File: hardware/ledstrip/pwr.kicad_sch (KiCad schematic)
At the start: 48 parts, among them J4 BMS connectors, J6 Header for STUSB4500 I2C, Q4 Q_PMOS, Q5 Q_NMOS, Q6 Q_NMOS, Q7 Q_NMOS, Q8 Q_NMOS, U5 BQ25703A, U6 STUSB4500QTR

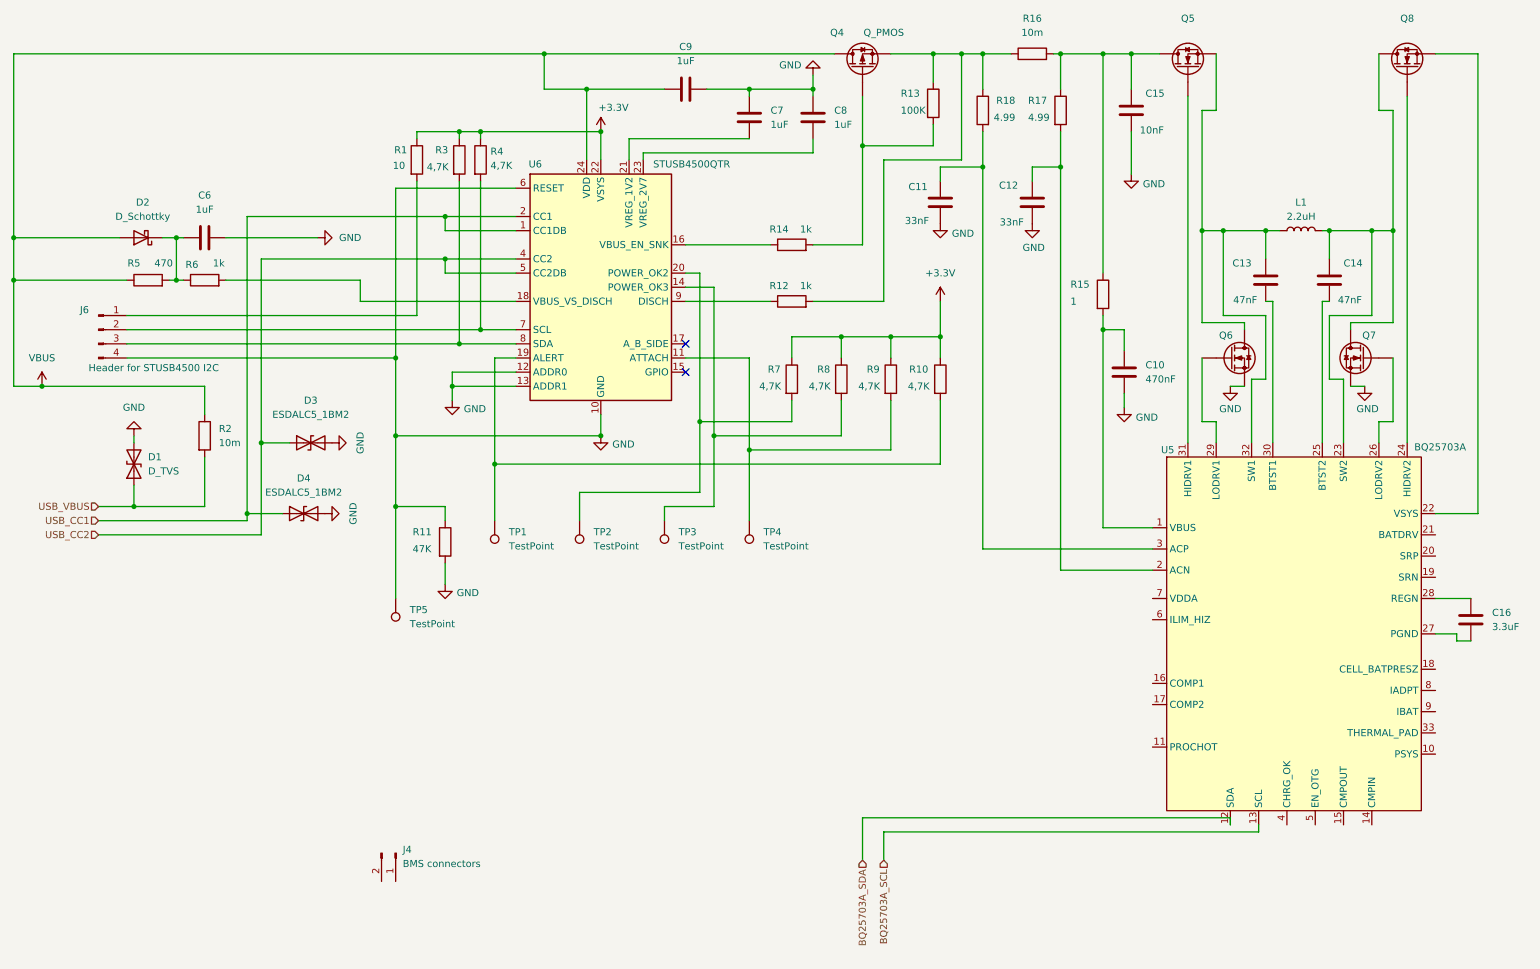
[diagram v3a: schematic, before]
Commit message: Splitted into multiple sheets.
BQ25703A integrated
buck converter OK
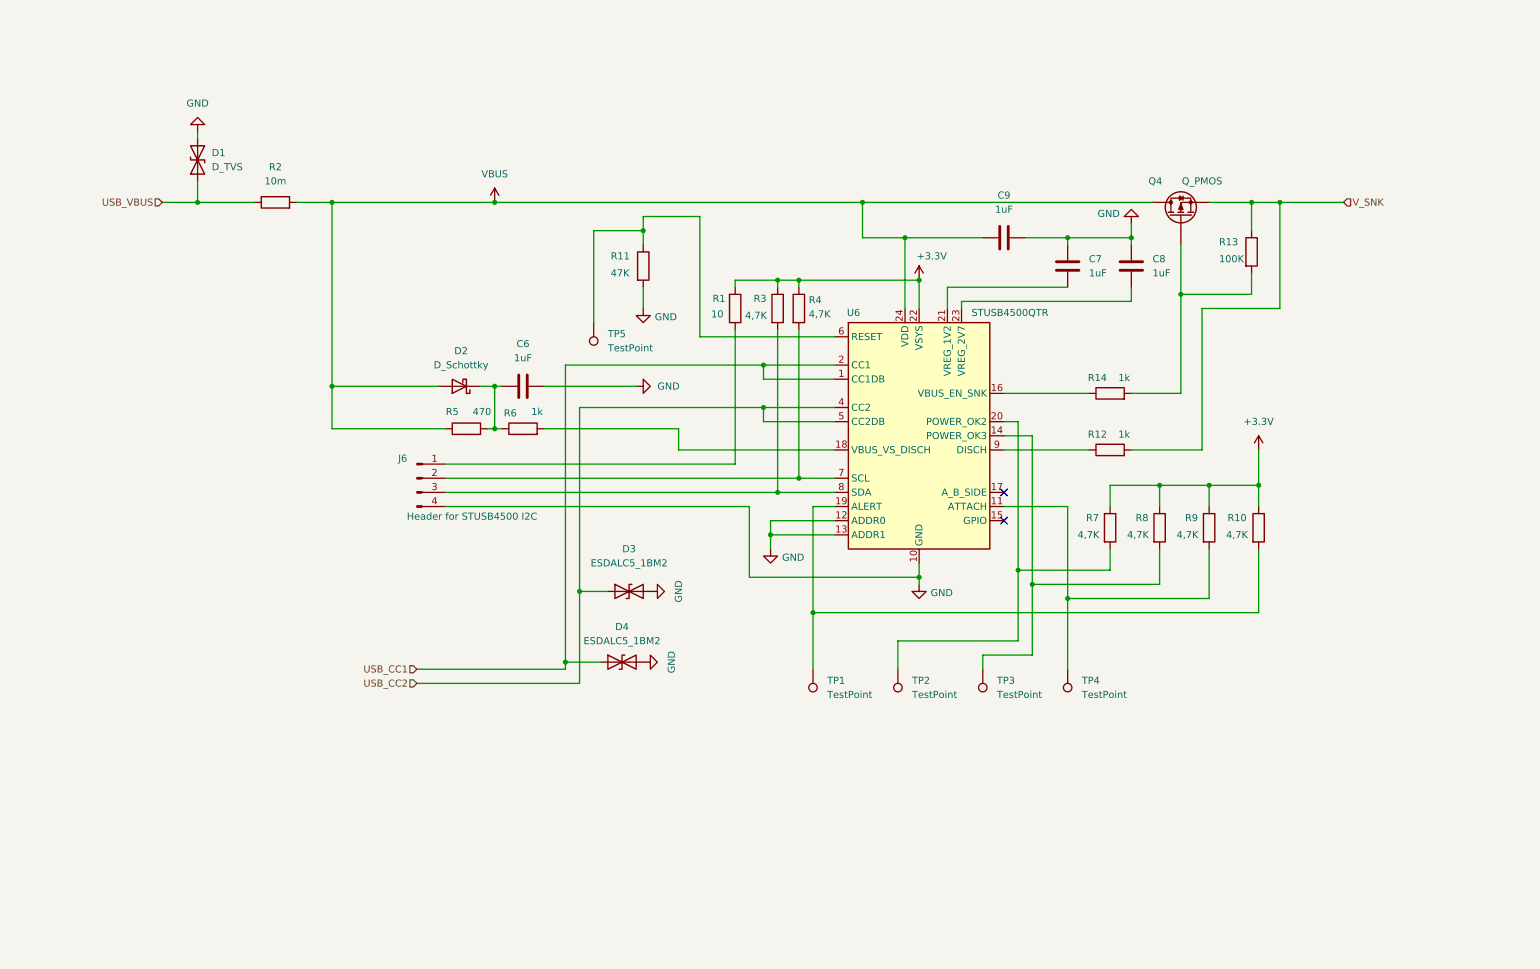
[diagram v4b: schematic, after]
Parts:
- removed C10: 470nF, Capacitor_SMD:C_0603_1608Metric, symbol Device:C
- removed C11, C12: 33nF, Capacitor_SMD:C_0603_1608Metric, symbol Device:C
- removed C13, C14: 47nF, Capacitor_SMD:C_0603_1608Metric, symbol Device:C
- removed C15: 10nF, Capacitor_SMD:C_0603_1608Metric, symbol Device:C
- removed C16: 3.3uF, Capacitor_SMD:C_0603_1608Metric, symbol Device:C
- removed J4: BMS connectors, Connector_PinHeader_2.54mm:PinHeader_1x02_P2.54mm_Vertical, symbol Connector:Conn_01x02_Pin
- removed L1: 2.2uH, ledstrip:L_Wurth_WE-LHMI-8030_9.7x8.5mm, symbol Device:L
- removed Q5, Q6, Q7, Q8: Q_NMOS, Package_SON:VSON-8_3.3x3.3mm_P0.65mm_NexFET, symbol Device:Q_NMOS
- removed R15: 1, Resistor_SMD:R_0805_2012Metric, symbol Device:R
- removed R16: 10m, Resistor_SMD:R_0805_2012Metric, symbol Device:R
- removed R17, R18: 4.99, Resistor_SMD:R_0805_2012Metric, symbol Device:R
- removed U5: BQ25703A, Package_DFN_QFN:Texas_RSN_WQFN-32-1EP_4x4mm_P0.4mm_EP2.8x2.8mm_ThermalVias, symbol ledstrip:BQ25703A
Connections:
- net GND: no longer R11.1, TP5.1, U6.6 (RESET)
- net USB_VBUS: now also R2.1; no longer R2.2
- net VBUS: now also R2.2; no longer R2.1
- net V_SNK: now reaches Q4.S, R12.2, R13.1
- new net: R11.1, TP5.1, U6.6 (RESET)
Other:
- moved on the sheet: C6, C7, C8, C9, D1, D2, D3, D4, J6, Q4, R1, R10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

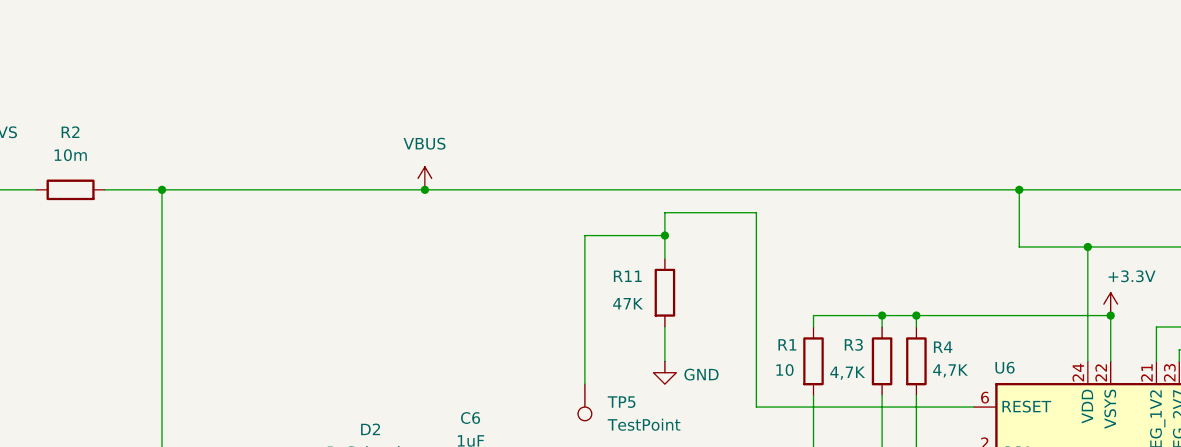
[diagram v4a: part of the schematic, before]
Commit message: Fix ERC errors.
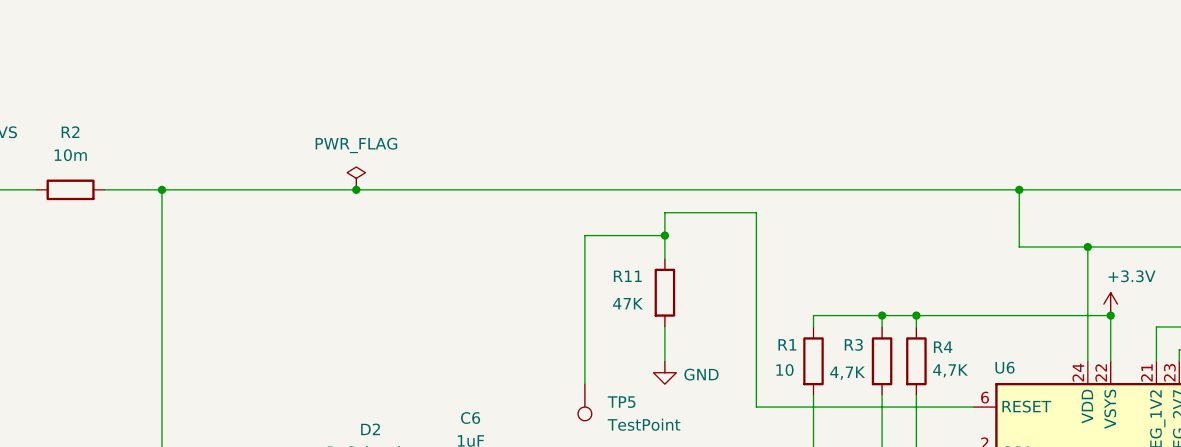
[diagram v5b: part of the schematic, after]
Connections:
- net VBUS: no longer names the net of C9.1, D2.2 (A), Q4.D, R2.2, R5.1, U6.24 (VDD)
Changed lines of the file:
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@@
 	)
 	(junction
+		(at 92.71 44.45)
+		(diameter 0)
+		(color 0 0 0 0)
+	)
+	(junction
 		(at 173.99 50.8)
 		(diameter 0)
@@
 	)
 	(junction
-		(at 100.33 44.45)
-		(diameter 0)
-		(color 0 0 0 0)
-	)
-	(junction
 		(at 71.12 44.45)
 		(diameter 0)
@@
 	(wire
 		(pts
-			(xy 100.33 44.45) (xy 166.37 44.45)
+			(xy 92.71 44.45) (xy 166.37 44.45)
 		)
 		(stroke
@@
 	(wire
 		(pts
-			(xy 71.12 44.45) (xy 100.33 44.45)
+			(xy 71.12 44.45) (xy 92.71 44.45)
 		)
 		(stroke
@@
 	)
 	(symbol
-		(lib_id "power:VBUS")
-		(at 100.33 44.45 0)
-		(unit 1)
-		(exclude_from_sim no)
-		(in_bom yes)
-		(on_board yes)
-		(dnp no)
-		(fields_autoplaced yes)
-		(property "Reference" "#PWR028"
-			(at 100.33 48.26 0)
-			(effects
-				(font
-					(size 1.27 1.27)
-				)
-				(hide yes)
-			)
-		)
-		(property "Value" "VBUS"
-			(at 100.33 39.37 0)
-			(effects
-				(font
-					(size 1.27 1.27)
-				)
-			)
-		)
-		(property "Footprint" ""
-			(at 100.33 44.45 0)
-			(effects
-				(font
-					(size 1.27 1.27)
-				)
-				(hide yes)
-			)
-		)
-		(property "Datasheet" ""
-			(at 100.33 44.45 0)
-			(effects
-				(font
-					(size 1.27 1.27)
-				)
-				(hide yes)
-			)
-		)
-		(property "Description" "Power symbol creates a global label with name \"VBUS\""
-			(at 100.33 44.45 0)
-			(effects
-				(font
-					(size 1.27 1.27)
-				)
-				(hide yes)
-			)
-		)
-		(pin "1"
-		)
-		(instances
-			(project "ledstrip"
-				(path "/dcb997ee-94c4-4df2-ba22-0e091735ddd7/b5cca531-fcff-4497-988a-ecdd56b3ddf9"
-					(reference "#PWR028")
-					(unit 1)
-				)
-			)
-		)
-	)
-	(symbol
 		(lib_id "Connector:Conn_01x04_Pin")
 		(at 86.36 93.98 0)
@@
 					(unit 1)
 				)
+			)
+		)
+	)
+	(symbol
+		(lib_id "power:PWR_FLAG")
+		(at 92.71 44.45 0)
+		(unit 1)
+		(exclude_from_sim no)
+		(in_bom yes)
+		(on_board yes)
+		(dnp no)
+		(fields_autoplaced yes)
+		(property "Reference" "#FLG02"
+			(at 92.71 42.545 0)
+			(effects
+				(font
+					(size 1.27 1.27)
+				)
+				(hide yes)
+			)
+		)
+		(property "Value" "PWR_FLAG"
+			(at 92.71 39.37 0)
+			(effects
+				(font
+					(size 1.27 1.27)
+				)
+			)
+		)
+		(property "Footprint" ""
+			(at 92.71 44.45 0)
+			(effects
+				(font
+					(size 1.27 1.27)
+				)
+				(hide yes)
+			)
+		)
+		(property "Datasheet" "~"
+			(at 92.71 44.45 0)
+			(effects
+				(font
+					(size 1.27 1.27)
+				)
+				(hide yes)
+			)
+		)
+		(property "Description" "Special symbol for telling ERC where power comes from"
+			(at 92.71 44.45 0)
+			(effects
+				(font
+					(size 1.27 1.27)
+				)
+				(hide yes)
+			)
+		)
+		(pin "1"
+		)
+		(instances
+			(project "ledstrip"
+				(path "/dcb997ee-94c4-4df2-ba22-0e091735ddd7/b5cca531-fcff-4497-988a-ecdd56b3ddf9"
+					(reference "#FLG02")
+					(unit 1)
+				)

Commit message: Fix last errors in schematics
Missing footprint, missing distributor link.
Updated project sym-lib-table for ERC checks.
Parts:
- D2: Disributor Link 1 https://www.mouser.com/ProductDetail/STMicroelectronics/BAT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 -> (none); Disributor Link 2 https://www.digikey.fr/fr/products/detail/stmicroelectronic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 -> (none); Distributor Link 1 (none) -> https://www.mouser.com/ProductDetail/STMicroelectronics/BAT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; Distributor Link 2 (none) -> https://www.digikey.fr/fr/products/detail/stmicroelectronic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
- Q4: Distributor Link 1 (none) -> https://www.mouser.com/ProductDetail/STMicroelectronics/STL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; Distributor Link 2 (none) -> https://www.digikey.com/en/products/detail/stmicroelectroni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
- TP1, TP2, TP3, TP4, TP5: footprint (none) -> TestPoint:TestPoint_Pad_1.0x1.0mm
- U6: Distributor Link 1 (none) -> https://www.mouser.com/ProductDetail/STMicroelectronics/STU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; Distributor Link 2 (none) -> https://www.digikey.com/en/products/detail/stmicroelectroni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
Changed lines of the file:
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@@
 			)
 		)
-		(property "Footprint" ""
+		(property "Footprint" "TestPoint:TestPoint_Pad_1.0x1.0mm"
 			(at 198.12 128.27 0)
 			(effects
@@
 			)
 		)
-		(property "Footprint" ""
+		(property "Footprint" "TestPoint:TestPoint_Pad_1.0x1.0mm"
 			(at 113.03 66.04 0)
 			(effects
@@
 			)
 		)
-		(property "Footprint" ""
+		(property "Footprint" "TestPoint:TestPoint_Pad_1.0x1.0mm"
 			(at 182.88 128.27 0)
 			(effects
@@
 			)
 		)
-		(property "Footprint" ""
+		(property "Footprint" "TestPoint:TestPoint_Pad_1.0x1.0mm"
 			(at 152.4 128.27 0)
 			(effects
@@
 			)
 		)
-		(property "Disributor Link 1" "https://www.mouser.com/ProductDetail/STMicroelectronics/BAT54JFILM?qs=iux7VCIsw51N9WI%2FM0S0Rw%3D%3D&srsltid=AfmBOooxKWAXyDgvP1UjimD1-9PbWrr97IdjW_4LbqipuO2zRGh0GC42"
+		(property "Distributor Link 1" "https://www.mouser.com/ProductDetail/STMicroelectronics/BAT54JFILM?qs=iux7VCIsw51N9WI%2FM0S0Rw%3D%3D&srsltid=AfmBOooxKWAXyDgvP1UjimD1-9PbWrr97IdjW_4LbqipuO2zRGh0GC42"
 			(at 93.98 77.47 0)
 			(effects
@@
 			)
 		)
-		(property "Disributor Link 2" "https://www.digikey.fr/fr/products/detail/stmicroelectronics/BAT54JFILM/1037673?srsltid=AfmBOopUPo3AAcuR1QLaM55k9Uwtr8ftSv0clmvJ2GOXMI3wjTavzLow"
+		(property "Distributor Link 2" "https://www.digikey.fr/fr/products/detail/stmicroelectronics/BAT54JFILM/1037673?srsltid=AfmBOopUPo3AAcuR1QLaM55k9Uwtr8ftSv0clmvJ2GOXMI3wjTavzLow"
 			(at 93.98 77.47 0)
 			(effects
@@
 			)
 		)
-		(property "Datasheet" "~"
+		(property "Datasheet" "https://www.st.com/resource/en/datasheet/stl6p3llh6.pdf"
 			(at 223.52 46.99 0)
 			(effects
@@
 			)
 		)
+		(property "Distributor Link 1" "https://www.mouser.com/ProductDetail/STMicroelectronics/STL6P3LLH6?qs=DqCdCwOw4%2F6Sn4l3cEaG7Q%3D%3D&srsltid=AfmBOor_CdWLVA3V0JAWOb-DG3H4EXYaOWWoltYAvPcJsUIQtpDcEfnR"
+			(at 223.52 46.99 90)
+			(effects
+				(font
+					(size 1.27 1.27)
+				)
+				(hide yes)
+			)
+		)
+		(property "Distributor Link 2" "https://www.digikey.com/en/products/detail/stmicroelectronics/STL6P3LLH6/5170838"
+			(at 223.52 46.99 90)
+			(effects
+				(font
+					(size 1.27 1.27)
+				)
+				(hide yes)
+			)
+		)
 		(pin "D"
 		)
@@
 		)
 		(property "Description" "Stand-alone USB PD controller (with sink Auto-run mode), QFN-24"
+			(at 176.53 86.36 0)
+			(effects
+				(font
+					(size 1.27 1.27)
+				)
+				(hide yes)
+			)
+		)
+		(property "Distributor Link 1" "https://www.mouser.com/ProductDetail/STMicroelectronics/STUSB4500QTR?qs=wUXugUrL1qyQbYMSzG1ujg%3D%3D&srsltid=AfmBOooDKZ9xpoXhvvlOwEhcpxAjVXgjEaXsOgnvZjSfZbs-iABblbdp"
+			(at 176.53 86.36 0)
+			(effects
+				(font
+					(size 1.27 1.27)
+				)
+				(hide yes)
+			)
+		)
+		(property "Distributor Link 2" "https://www.digikey.com/en/products/detail/stmicroelectronics/STUSB4500QTR/9092189"
 			(at 176.53 86.36 0)
 			(effects
@@
 			)
 		)
-		(property "Footprint" ""
+		(property "Footprint" "TestPoint:TestPoint_Pad_1.0x1.0mm"
 			(at 167.64 128.27 0)
 			(effects
